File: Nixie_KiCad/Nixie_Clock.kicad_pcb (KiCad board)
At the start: 2 copper layers, 140 x 60 mm, 22 parts, among them U1 K155ID1, U10 K155ID1, U11 IN-14, U12 DS3231, U2 IN-14, U3 K155ID1, U4 IN-14, U5 K155ID1, U6 IN-3, U7 PS_V2H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

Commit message: Updated BOM
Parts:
- moved R1 165.8 mm to (109.7, 83.3)
- moved R2 165.8 mm to (114.7, 83.3)
- moved R3 165.8 mm to (121.7, 90.8)
- moved R7 165.8 mm to (119.7, 87.3)
- moved U1 165.8 mm to (79.7, 123.3)
- moved U12 165.8 mm to (164.5, 104.4)
- moved U2 165.8 mm to (79.7, 103.3)
- moved U3 165.8 mm to (109.7, 123.3)
- moved U4 165.8 mm to (109.7, 103.3)
- moved U7 165.8 mm to (84.7, 88.3)
- moved A1 165.8 mm to (145.7, 76.3)
- moved R4 165.8 mm to (129.7, 90.8)
- moved R5 165.8 mm to (137.7, 90.8)
- moved R6 165.8 mm to (139.7, 87.3)
- moved R8 165.8 mm to (133.7, 83.3)
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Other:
- board text added: "github.com/haXoru5/nixie_clock"

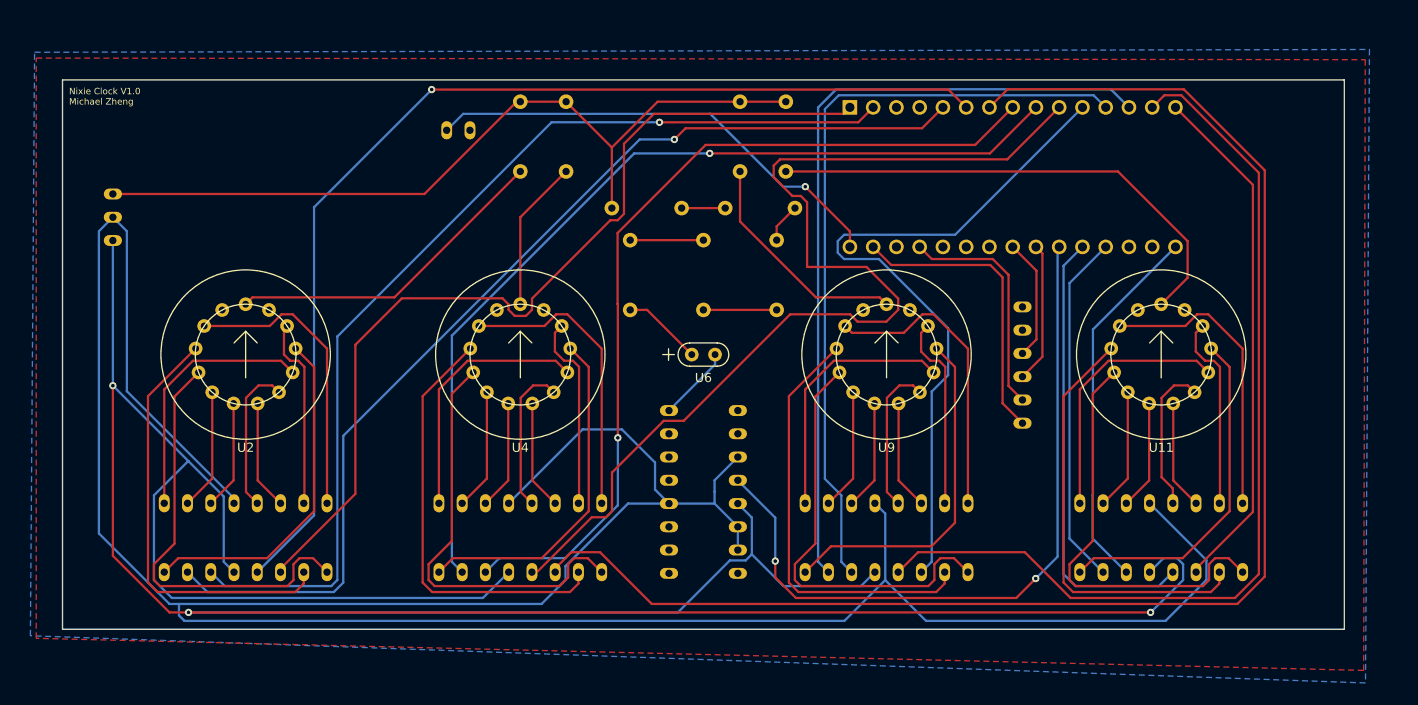
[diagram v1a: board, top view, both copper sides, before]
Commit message: Added Drill Holes
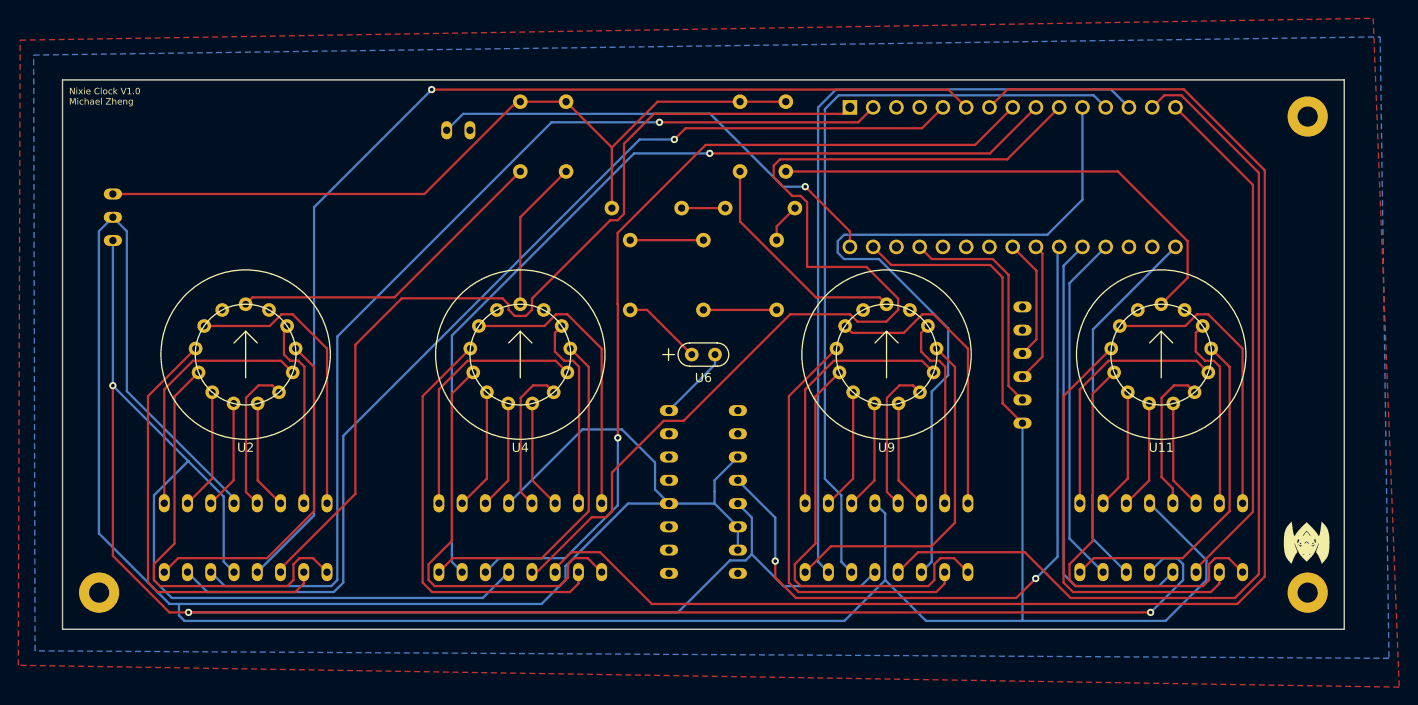
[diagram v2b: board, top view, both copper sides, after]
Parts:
- added G***: LOGO, Nixie_Clock_Footprint:haxorus, F.Cu at (195.6, 123.8)
- added REF**: MountingHole_2.2mm_M2_Pad, MountingHole:MountingHole_2.2mm_M2_Pad, F.Cu at (195.7, 129.3)
- added e: MountingHole_2.2mm_M2_Pad, MountingHole:MountingHole_2.2mm_M2_Pad, F.Cu at (63.7, 129.3)
- added e: MountingHole_2.2mm_M2_Pad, MountingHole:MountingHole_2.2mm_M2_Pad, F.Cu at (195.7, 77.3)
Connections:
- A1 pad 29: Net-(A1-Pad29) -> GND
- A1 pad 4: Net-(A1-Pad29) -> GND
- U12 pad 6: Net-(A1-Pad29) -> GND
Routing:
- net GND: track 325.0 -> 379.0 mm
- net Net-(A1-Pad29): track 32.3 -> 0.00 mm
- net M1A: track 77.4 -> 83.3 mm
- added copper zone on F.Cu, net (none)
- removed copper zone on F.Cu, net GND

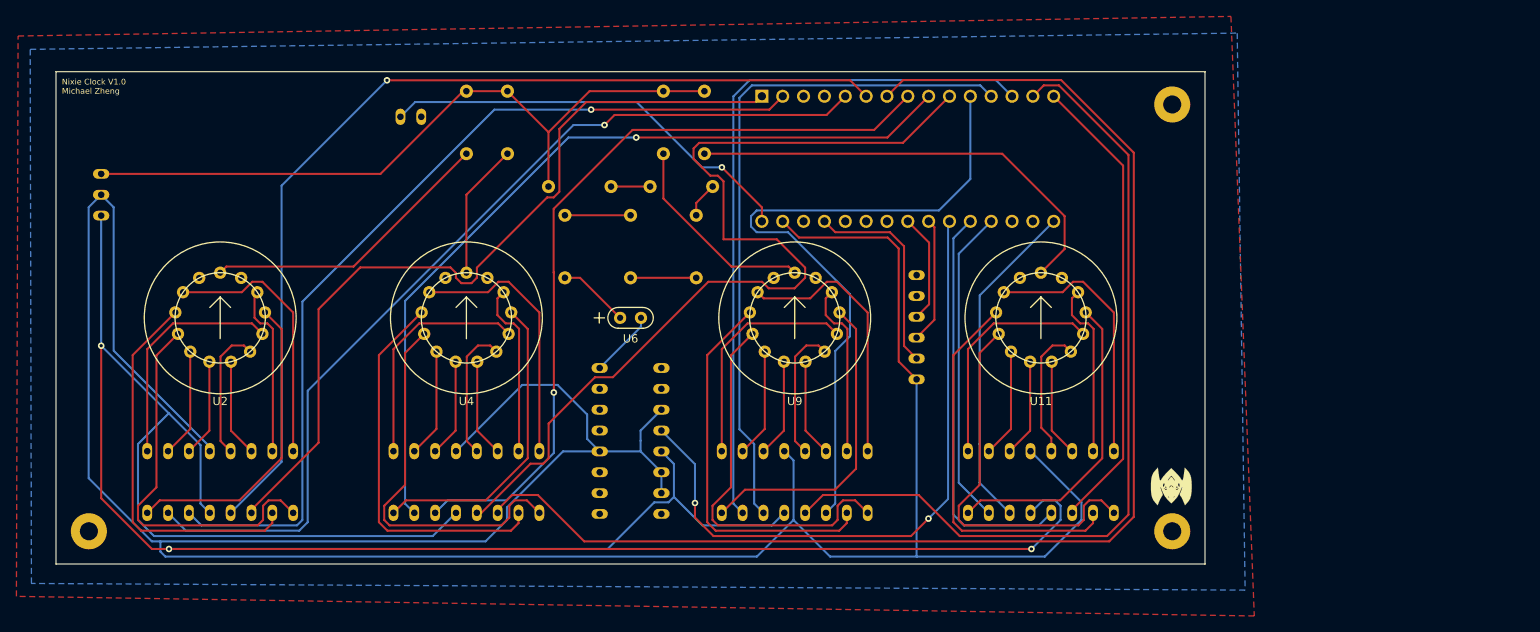
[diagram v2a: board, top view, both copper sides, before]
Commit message: added filter capacitors
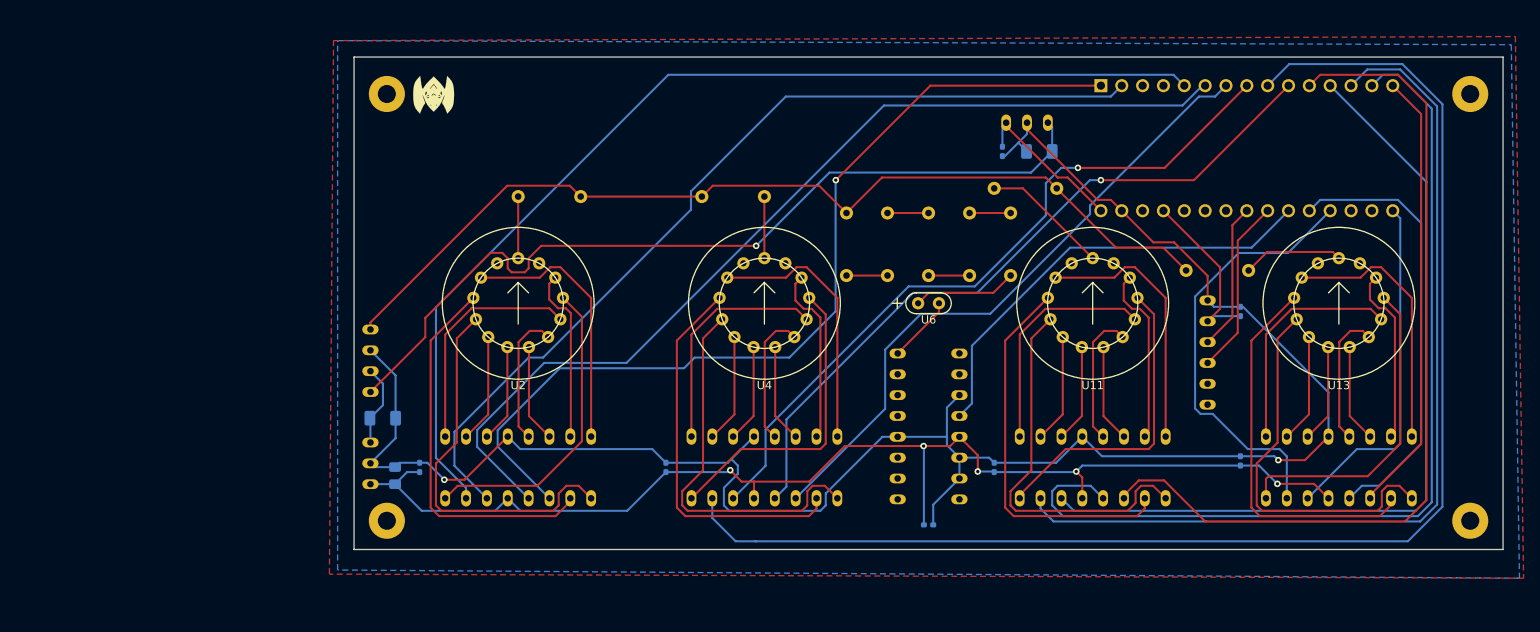
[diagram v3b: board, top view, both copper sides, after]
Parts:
- removed the REF** at (195.7, 129.3)
- removed the e at (63.7, 129.3)
- removed the e at (195.7, 77.3)
- added C1: 100nF, Capacitor_SMD:C_0402_1005Metric_Pad0.74x0.62mm_HandSolder, B.Cu at (104.0, 121.5)
- added C10: 100nF, Capacitor_SMD:C_0402_1005Metric_Pad0.74x0.62mm_HandSolder, B.Cu at (204.0, 102.5)
- added C2: 100nF, Capacitor_SMD:C_0402_1005Metric_Pad0.74x0.62mm_HandSolder, B.Cu at (134.0, 121.5)
- added C3: 100nF, Capacitor_SMD:C_0402_1005Metric_Pad0.74x0.62mm_HandSolder, B.Cu at (166.0, 128.5)
- added C4: 100nF, Capacitor_SMD:C_0402_1005Metric_Pad0.74x0.62mm_HandSolder, B.Cu at (175.0, 83.0)
- added C5: 0.33uF, Capacitor_SMD:C_1206_3216Metric_Pad1.33x1.80mm_HandSolder, B.Cu at (179.5, 83.0)
- added C6: 100nF, Capacitor_SMD:C_0402_1005Metric_Pad0.74x0.62mm_HandSolder, B.Cu at (174.0, 121.5)
- added C7: 100nF, Capacitor_SMD:C_0402_1005Metric_Pad0.74x0.62mm_HandSolder, B.Cu at (204.0, 120.7)
- added C8: 0.33uF, Capacitor_SMD:C_1206_3216Metric_Pad1.33x1.80mm_HandSolder, B.Cu at (99.5, 115.5)
- added C9: 10uF, Capacitor_SMD:C_0805_2012Metric_Pad1.18x1.45mm_HandSolder, B.Cu at (101.0, 122.5)
- added REF**: MountingHole_2.2mm_M2_Pad, MountingHole:MountingHole_2.2mm_M2_Pad, F.Cu at (232.0, 76.0)
- added REF**: MountingHole_2.2mm_M2_Pad, MountingHole:MountingHole_2.2mm_M2_Pad, F.Cu at (232.0, 128.0)
- added REF**: MountingHole_2.2mm_M2_Pad, MountingHole:MountingHole_2.2mm_M2_Pad, F.Cu at (100.0, 76.0)
- added U13: IN-14, Nixie_Clock_Footprint:IN-14, F.Cu at (216.0, 101.5)
- added U14: DS3231, Nixie_Clock_Footprint:DS3231, B.Cu at (200.0, 107.5)
- added e: MountingHole_2.2mm_M2_Pad, MountingHole:MountingHole_2.2mm_M2_Pad, F.Cu at (100.0, 128.0)
- U12: value DS3231 -> K155ID1; footprint Nixie_Clock_Footprint:DS3231 -> Nixie_Clock_Footprint:K155ID1
- U7: value PS_V2H -> L7812CV; footprint Nixie_Clock_Footprint:PS_V2H -> Nixie_Clock_Footprint:SIP-3
- U8: value K155ID1 -> PS_V2H; footprint Nixie_Clock_Footprint:K155ID1 -> Nixie_Clock_Footprint:PS_V2H
- U9: value IN-14 -> NCV7805BTG; footprint Nixie_Clock_Footprint:IN-14 -> Nixie_Clock_Footprint:SIP-3; moved to B.Cu
- moved G*** 101.8 mm to (105.7, 76.1)
- moved U7 93.7 mm to (178.0, 79.5)
- moved R9 67.8 mm to (205.0, 97.5), turned to 180 degrees
- moved U9 54.6 mm to (98.0, 121.0), turned to 270 degrees
- moved R3 54.3 mm to (176.0, 90.5)
- moved U12 54.2 mm to (216.0, 121.5), turned to 180 degrees
- moved U8 53.8 mm to (98.0, 108.5), turned to 270 degrees
- moved A1 41.3 mm to (187.0, 75.0)
- moved R4 41.3 mm to (171.0, 90.5)
- moved R8 40.5 mm to (174.0, 87.5), turned to 0 degrees
- moved R7 36.5 mm to (156.0, 90.5), turned to 270 degrees
- moved U5 36.4 mm to (166.0, 116.5)
- moved U6 36.4 mm to (166.0, 101.5)
- moved U1 36.4 mm to (116.0, 121.5)
- moved U2 36.4 mm to (116.0, 101.5)
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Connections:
- A1 pad 22: Net-(A1-Pad22) -> SCL
- A1 pad 23: Net-(A1-Pad23) -> SDA
- A1 pad 30: +12V -> Net-(A1-Pad30)
- U10 pad 3: M2A -> M1A
- U10 pad 4: M2D -> M1D
- U10 pad 6: M2B -> M1B
- U10 pad 7: M2C -> M1C
- U11 pad 1: Net-(R9-Pad1) -> Net-(R8-Pad1)
- U12 pad 3: Net-(A1-Pad23) -> M2A
- U12 pad 4: Net-(A1-Pad22) -> M2D
- U12 pad 5: Net-(A1-Pad27) -> +5V
- U12 pad 6: GND -> M2B
- U7 pad 1: Earth -> +12V
- U7 pad 2: +12V -> GND
- U7 pad 3: +170V -> Net-(A1-Pad30)
- U8 pad 1: Net-(U8-Pad1) -> +170V
- U8 pad 2: Net-(U8-Pad2) -> GND
- U8 pad 3: M1A -> Net-(C8-Pad2)
- U8 pad 4: M1D -> +12V
- U9 pad 1: Net-(R8-Pad1) -> Net-(C8-Pad2)
- U9 pad 2: Net-(U9-Pad2) -> GND
- U9 pad 3: Net-(U8-Pad15) -> +5V
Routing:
- net +5V: track 328.7 -> 148.0 mm, vias 3 -> 5
- net GND: track 379.0 -> 240.1 mm, vias 0 -> 2
- net H2A: track 161.1 -> 78.1 mm
- net H2C: track 100.4 -> 167.8 mm, vias 1 -> 0
- net +12V: track 51.8 -> 103.7 mm
- net Net-(U12-Pad1): track 0.00 -> 46.9 mm
- net Net-(U8-Pad2): track 46.8 -> 0.00 mm
- net Net-(U8-Pad1): track 46.8 -> 0.00 mm
- net Net-(U12-Pad2): track 0.00 -> 46.5 mm
- net Net-(R9-Pad1): track 55.1 -> 12.2 mm
- net Net-(U12-Pad8): track 0.00 -> 39.1 mm
- net Net-(U8-Pad8): track 38.5 -> 0.00 mm
- net Net-(U8-Pad16): track 33.0 -> 0.00 mm
- net Net-(U12-Pad16): track 0.00 -> 32.4 mm
- net Net-(R1-Pad1): track 36.0 -> 7.50 mm
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- added copper zone on F.Cu, net GND
- removed copper zone on F.Cu, net (none)
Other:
- board text added: "+12V"
- board text added: "+170V"
- board text added: "+5V"
- board text added: "D0"
- board text added: "GND"
- board text added: "Nixie Clock V1.1 Michael Zheng"
- board text removed: "Nixie Clock V1.0 Michael Zheng"

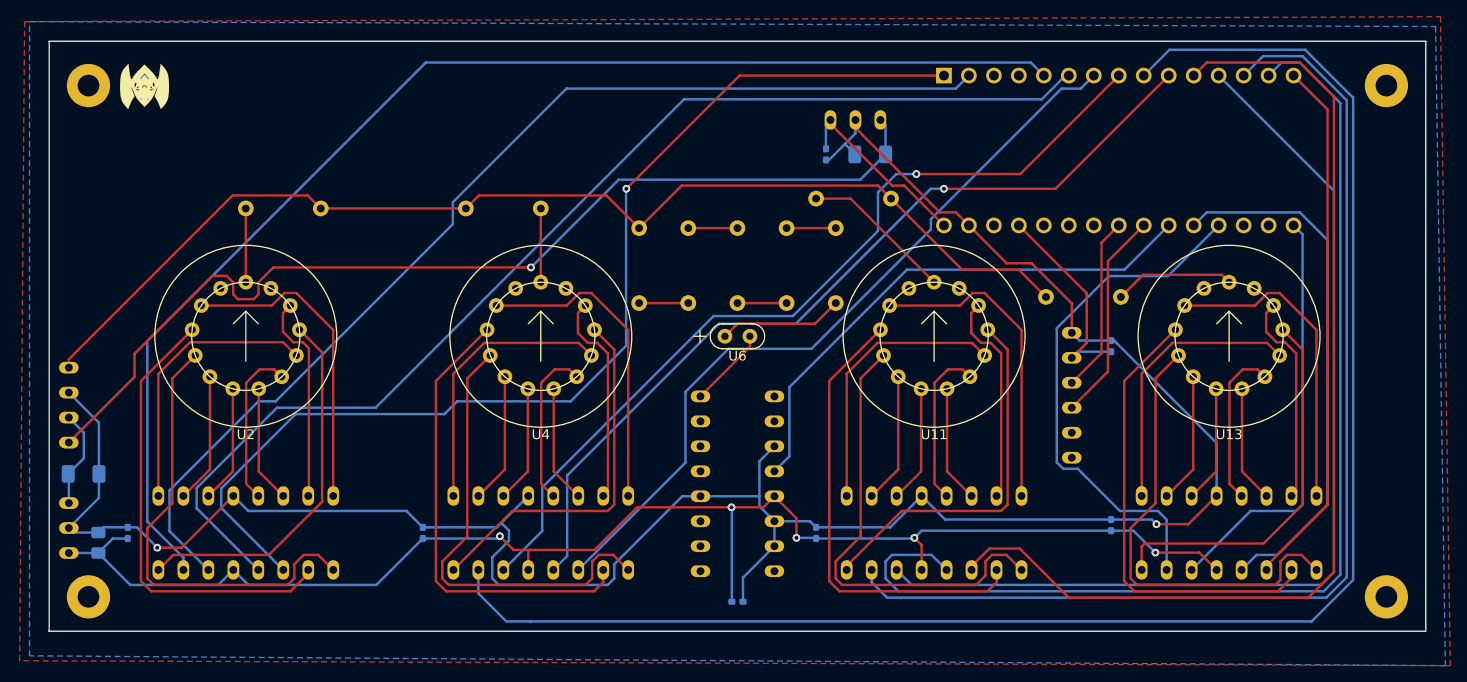
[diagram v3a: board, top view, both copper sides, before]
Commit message: updated footprints
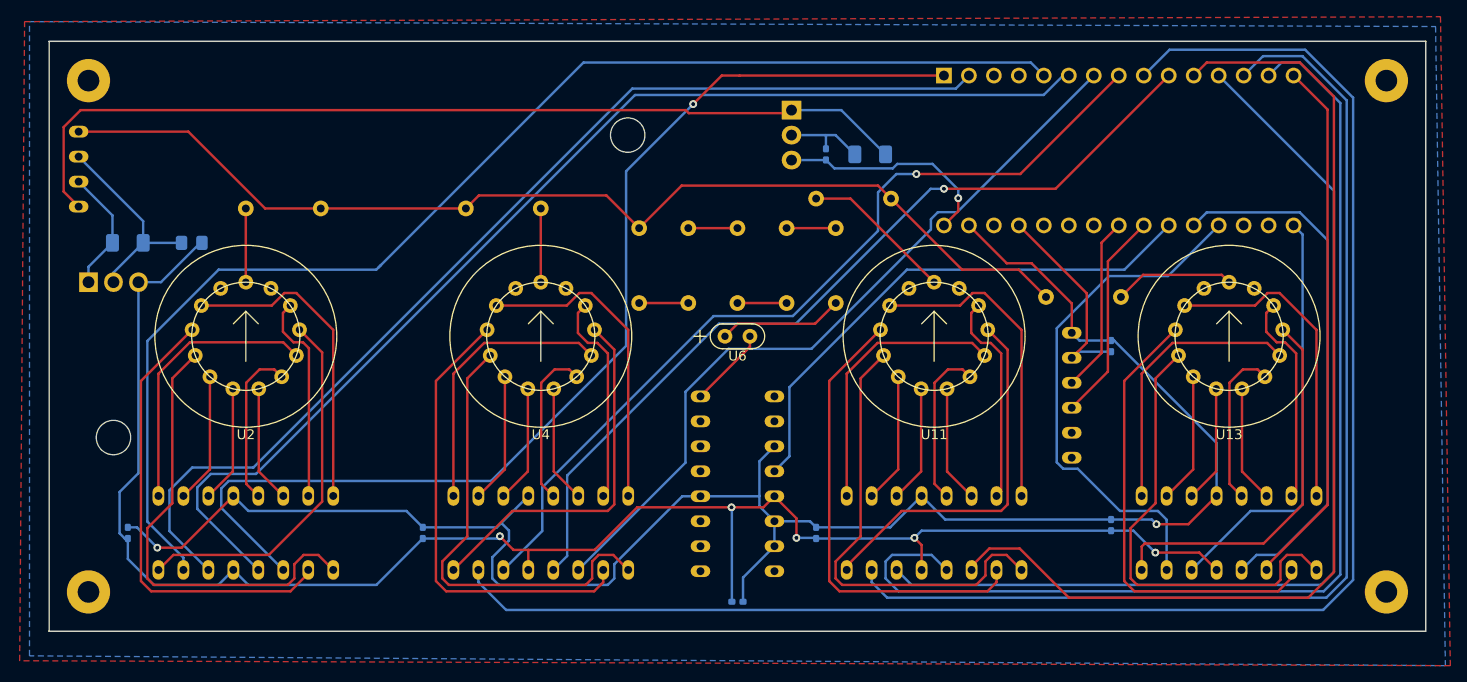
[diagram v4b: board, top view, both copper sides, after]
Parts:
- removed G***: LOGO, Nixie_Clock_Footprint:haxorus
- removed the REF** at (232.0, 76.0)
- removed the REF** at (232.0, 128.0)
- removed the REF** at (100.0, 76.0)
- removed e: MountingHole_2.2mm_M2_Pad, MountingHole:MountingHole_2.2mm_M2_Pad
- added REF**: MountingHole_2.2mm_M2_Pad, MountingHole:MountingHole_2.2mm_M2_Pad, F.Cu at (232.0, 75.5)
- added REF**: MountingHole_2.2mm_M2_Pad, MountingHole:MountingHole_2.2mm_M2_Pad, F.Cu at (232.0, 127.5)
- added REF**: MountingHole_2.2mm_M2_Pad, MountingHole:MountingHole_2.2mm_M2_Pad, F.Cu at (100.0, 127.5)
- added REF**: MountingHole_2.2mm_M2_Pad, MountingHole:MountingHole_2.2mm_M2_Pad, F.Cu at (100.0, 75.5)
- U7: footprint Nixie_Clock_Footprint:SIP-3 -> Package_TO_SOT_THT:TO-220-3_Horizontal_TabDown
- U9: value NCV7805BTG -> NJM78M05FA‎; footprint Nixie_Clock_Footprint:SIP-3 -> Package_TO_SOT_THT:TO-220F-3_Horizontal_TabDown
- moved C9 31.9 mm to (110.5, 92.0), turned to 180 degrees
- moved U9 25.1 mm to (100.0, 96.0), turned to 0 degrees
- moved U8 24.0 mm to (99.0, 84.5)
- moved C8 23.9 mm to (104.0, 92.0)
- moved U7 6.58 mm to (171.5, 78.5), turned to 270 degrees
- turned C4 to 90 degrees
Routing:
- net +5V: track 148.0 -> 175.7 mm
- net GND: track 240.1 -> 223.2 mm
- net +12V: track 103.7 -> 95.1 mm, vias 1 -> 0
- net +170V: track 116.1 -> 110.0 mm
- net Net-(A1-Pad30): track 19.3 -> 22.8 mm, vias 0 -> 1
- net Net-(C8-Pad2): track 10.0 -> 12.7 mm
- net H2C: track 167.8 -> 166.1 mm
- net H1B: track 109.8 -> 108.5 mm
- net H1A: track 111.1 -> 112.2 mm

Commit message: generated gerbers
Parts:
- added G***: LOGO, Nixie_Clock_Footprint:haxorus_large, F.Cu at (127.5, 81.5)
